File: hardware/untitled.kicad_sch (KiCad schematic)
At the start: 40 parts, among them J5 DCJ200-10-A-K1-K, J6 USB4105-GF-A, SW1 RA1113112R, SW2 SW_Push, SW3 SW_Push, U3 NCP1117ST33T3G, U4 ESP32-S3-WROOM-1-N8R8, U5 USBLC6-2SC6

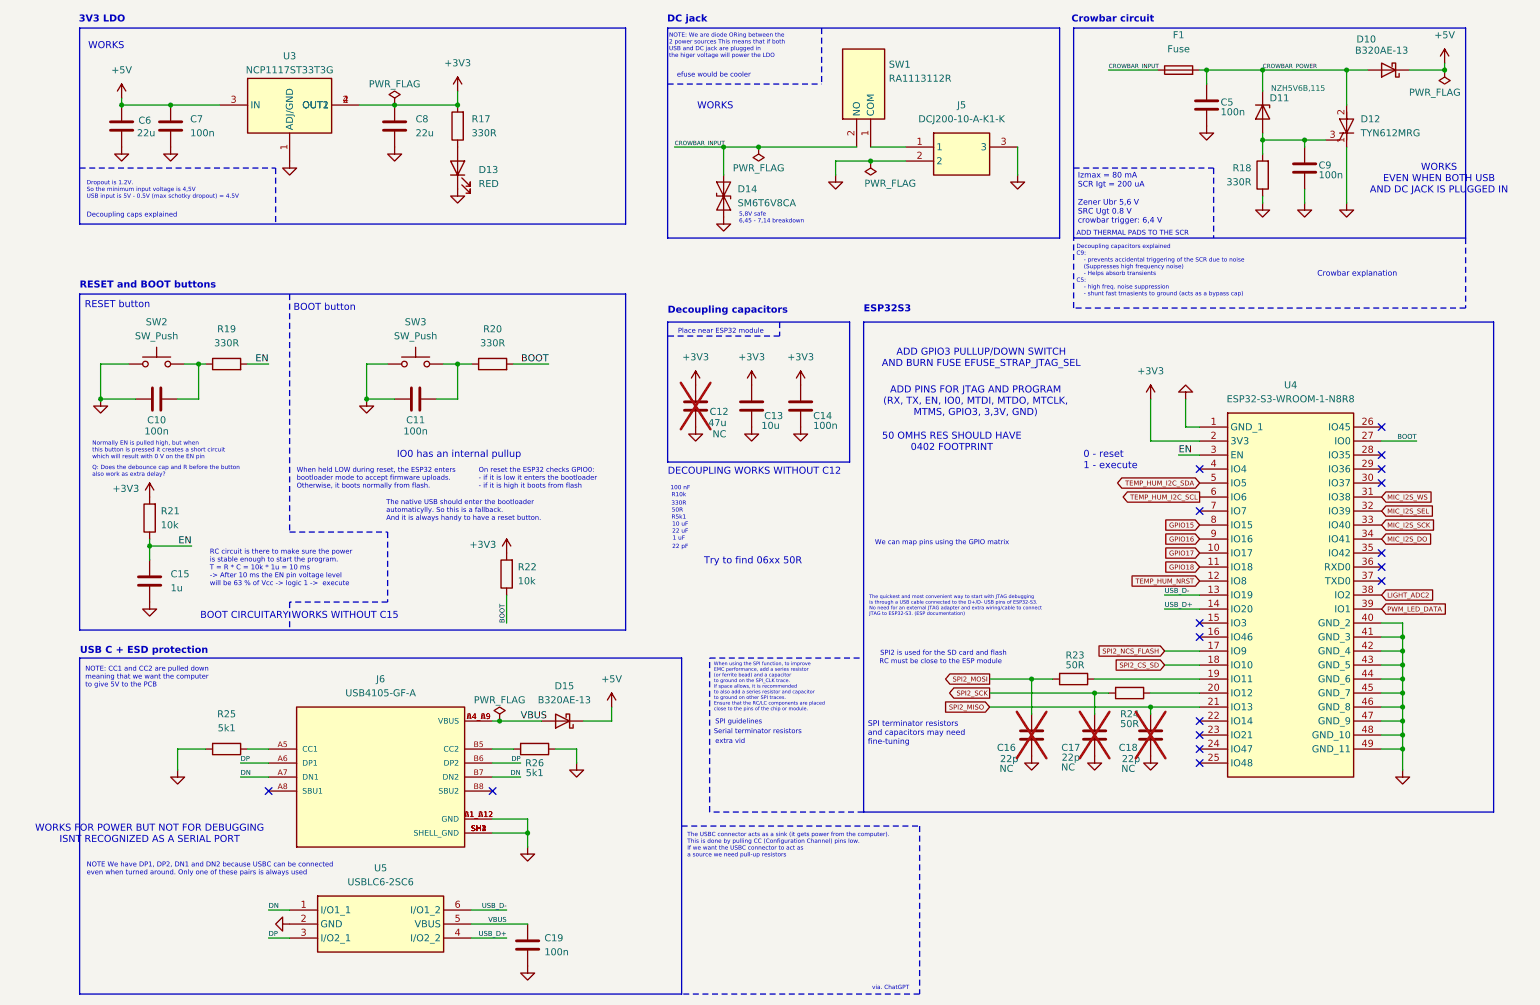
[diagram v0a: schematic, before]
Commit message: Tried to prevent crosstalk, fixed silkscreen, changes to fit DFM
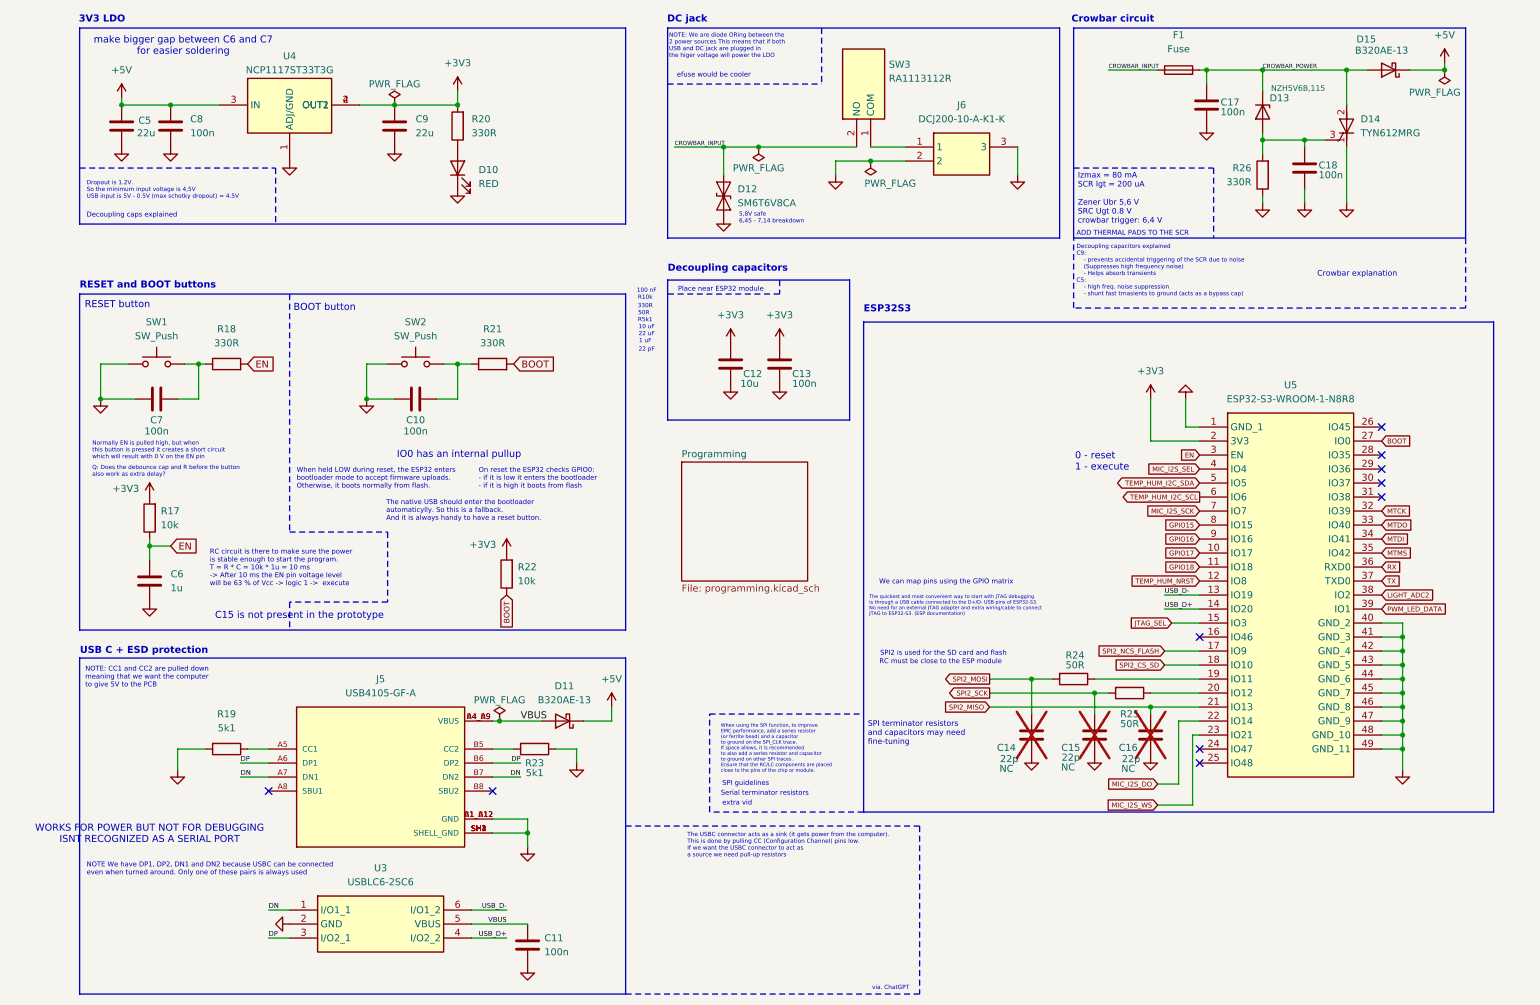
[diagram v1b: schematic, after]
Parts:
- removed C12: 47u, Capacitor_SMD:C_1206_3216Metric_Pad1.33x1.80mm_HandSolder, symbol Device:C
- R24: renamed from R23; footprint Resistor_SMD:R_0603_1608Metric_Pad0.98x0.95mm_HandSolder -> Resistor_SMD:R_0402_1005Metric_Pad0.72x0.64mm_HandSolder
- R25: renamed from R24; footprint Resistor_SMD:R_0603_1608Metric_Pad0.98x0.95mm_HandSolder -> Resistor_SMD:R_0402_1005Metric_Pad0.72x0.64mm_HandSolder
- renumbered C11 to C10, C19 to C11, C13 to C12, C14 to C13, C16 to C14, C17 to C15, C18 to C16, C5 to C17, C9 to C18, C6 to C5, C15 to C6, C10 to C7, C7 to C8, C8 to C9, D13 to D10, D15 to D11, D14 to D12, D11 to D13, D12 to D14, D10 to D15, J6 to J5, J5 to J6, R21 to R17, R19 to R18, R25 to R19, R17 to R20, R20 to R21, R26 to R23, R18 to R26, SW2 to SW1, SW3 to SW2, SW1 to SW3, U5 to U3, U3 to U4, U4 to U5
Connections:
- net MIC_I2S_DO: now also U5.22 (IO14); no longer U5.34 (IO41)
- net MIC_I2S_SCK: now also U5.7 (IO7); no longer U5.33 (IO40)
- net MIC_I2S_SEL: now also U5.4 (IO4); no longer U5.32 (IO39)
- net MIC_I2S_WS: now also U5.23 (IO21); no longer U5.31 (IO38)
- net JTAG_SEL: now reaches U5.15 (IO3)
- net MTMS: now reaches U5.35 (IO42)
- net RX: now reaches U5.36 (RXD0)
- net TX: now reaches U5.37 (TXD0)
- new net MTCK: U5.32 (IO39)
- new net MTDI: U5.34 (IO41)
- new net MTDO: U5.33 (IO40)
- no-connect marks 17 -> 10
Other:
- added sheet Programming (programming.kicad_sch)
- note added: "C15 is not present in the prototype"
- note added: "make bigger gap between C6 and C7 for easier soldering"
- note removed: "50 OMHS RES SHOULD HAVE 0402 FOOTPRINT"
- note removed: "ADD GPIO3 PULLUP/DOWN SWITCH AND BURN FUSE EFUSE_STRAP_JTAG_SEL"
- note removed: "ADD PINS FOR JTAG AND PROGRAM (RX, TX, EN, IO0, MTDI, MTDO, MTCLK, MTMS, GPIO3, 3,3V, GND)"
- note removed: "BOOT CIRCUITARY WORKS WITHOUT C15"
- note removed: "DECOUPLING WORKS WITHOUT C12"
- note removed: "Try to find 06xx 50R"
- note removed: "WORKS"
- note removed: "WORKS EVEN WHEN BOTH USB AND DC JACK IS PLUGGED IN"
- moved on the sheet: C12, C13
